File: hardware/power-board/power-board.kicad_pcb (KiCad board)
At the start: 2 copper layers, 144 parts, among them IC101 TCAN332DR, IC102 NUP2105LT1G, IC103 STM32C092KCT6, IC104 TPS62933DRLR, IC201 BQ7694202PFBR, IC301 BQ25798RQMR, IC302 CYPD3177-24LQXQ, J101 CAN, J102 SYSCTL, J103 TC2050, J201 XT60 BAT, J202 BALANCE, J203 NTC CELL, J204 POWER BTN, J205 XT30 LEFT, J206 XT30 RIGHT, J207 XT30 CARRIER, J301 USB4125-GF-A, Q101 2N7002, Q201 BSC010N04LSATMA1, Q202 DMP3099L, Q203 BSC010N04LSATMA1, Q204 BCP56, Q301 BSS138-7-F, Y101 Crystal_GND24

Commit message: updated power node pcb
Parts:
- moved R206 61.5 mm to (119.5, 72.5)
- moved IC201 60.3 mm to (105.0, 85.0)
- moved R203 56.0 mm to (119.5, 75.0)
- moved R211 55.6 mm to (113.0, 67.0), turned to 90 degrees
- moved R212 53.9 mm to (119.5, 80.0)
- moved R210 52.5 mm to (119.5, 77.5)
- moved R213 48.2 mm to (117.0, 68.0)
- moved R219 46.6 mm to (108.0, 71.0)
- moved R202 45.3 mm to (102.0, 67.0), turned to 90 degrees
- moved Q202 45.2 mm to (123.0, 77.0)
- moved R205 45.2 mm to (93.0, 68.0)
- moved TP302 42.4 mm to (87.0, 95.0)
- moved R214 42.3 mm to (123.0, 82.0)
- moved C206 42.1 mm to (125.0, 63.0)
- moved Q204 37.0 mm to (104.0, 70.5)
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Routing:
- added copper zone on F.Cu, net /BAT+
- added copper zone on F.Cu, net /PACK+
- added copper zone on B.Cu, net GND
- added copper zone on F.Cu, net GND
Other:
- board outline added: 65 x 65 mm

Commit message: changed power board to 4 layers
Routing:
- removed copper zone on F.Cu, net /BAT+
- removed copper zone on F.Cu, net /PACK+
- removed copper zone on B.Cu, net GND
- removed copper zone on F.Cu, net GND
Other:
- board outline removed
- copper layers 2 -> 4

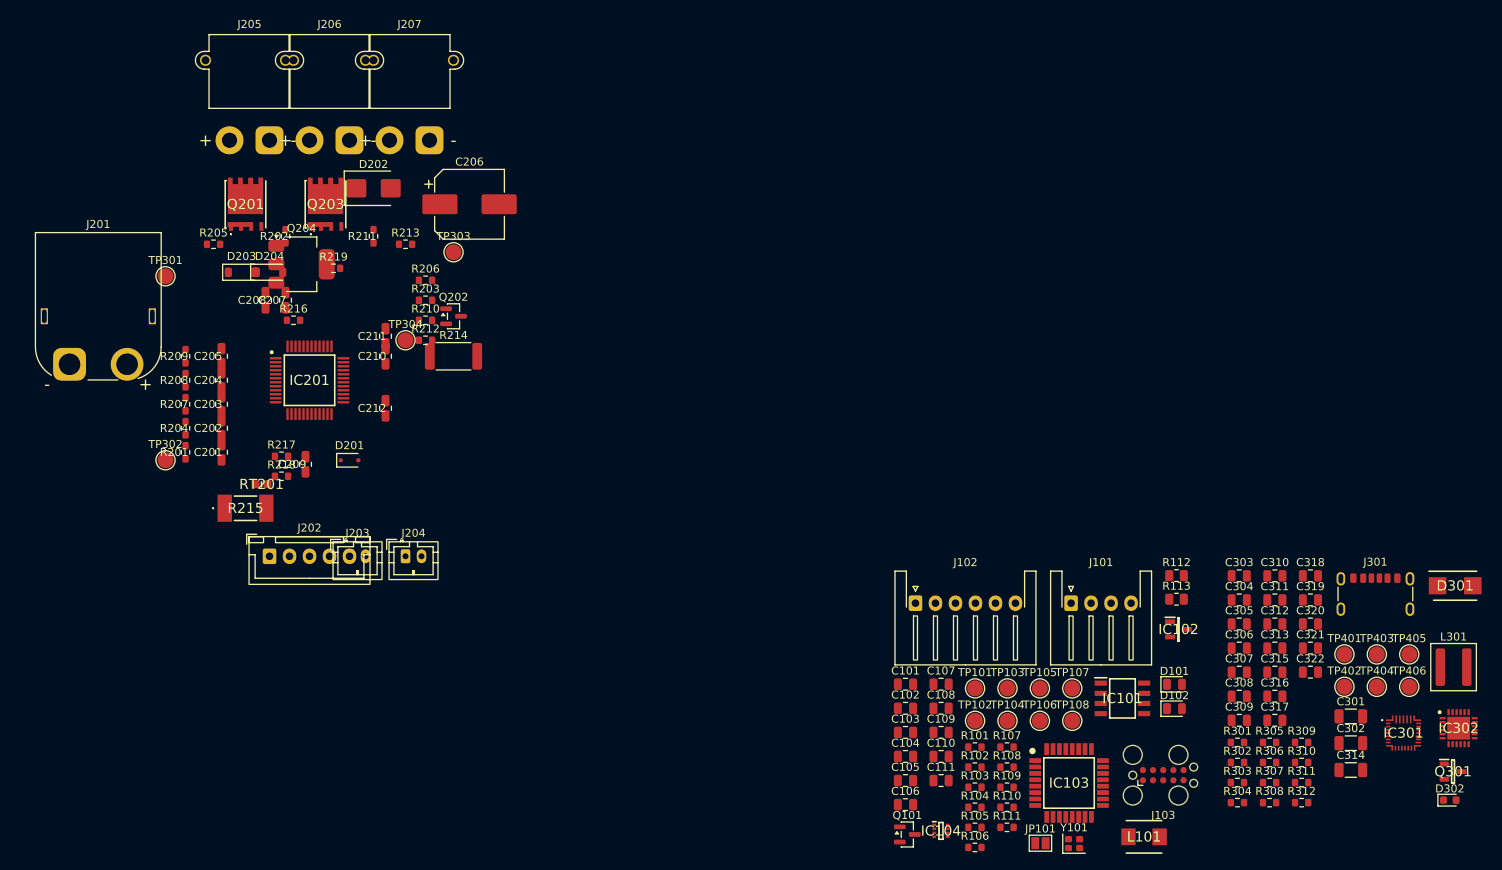
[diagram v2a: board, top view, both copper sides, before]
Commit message: placed bms and power path on power board
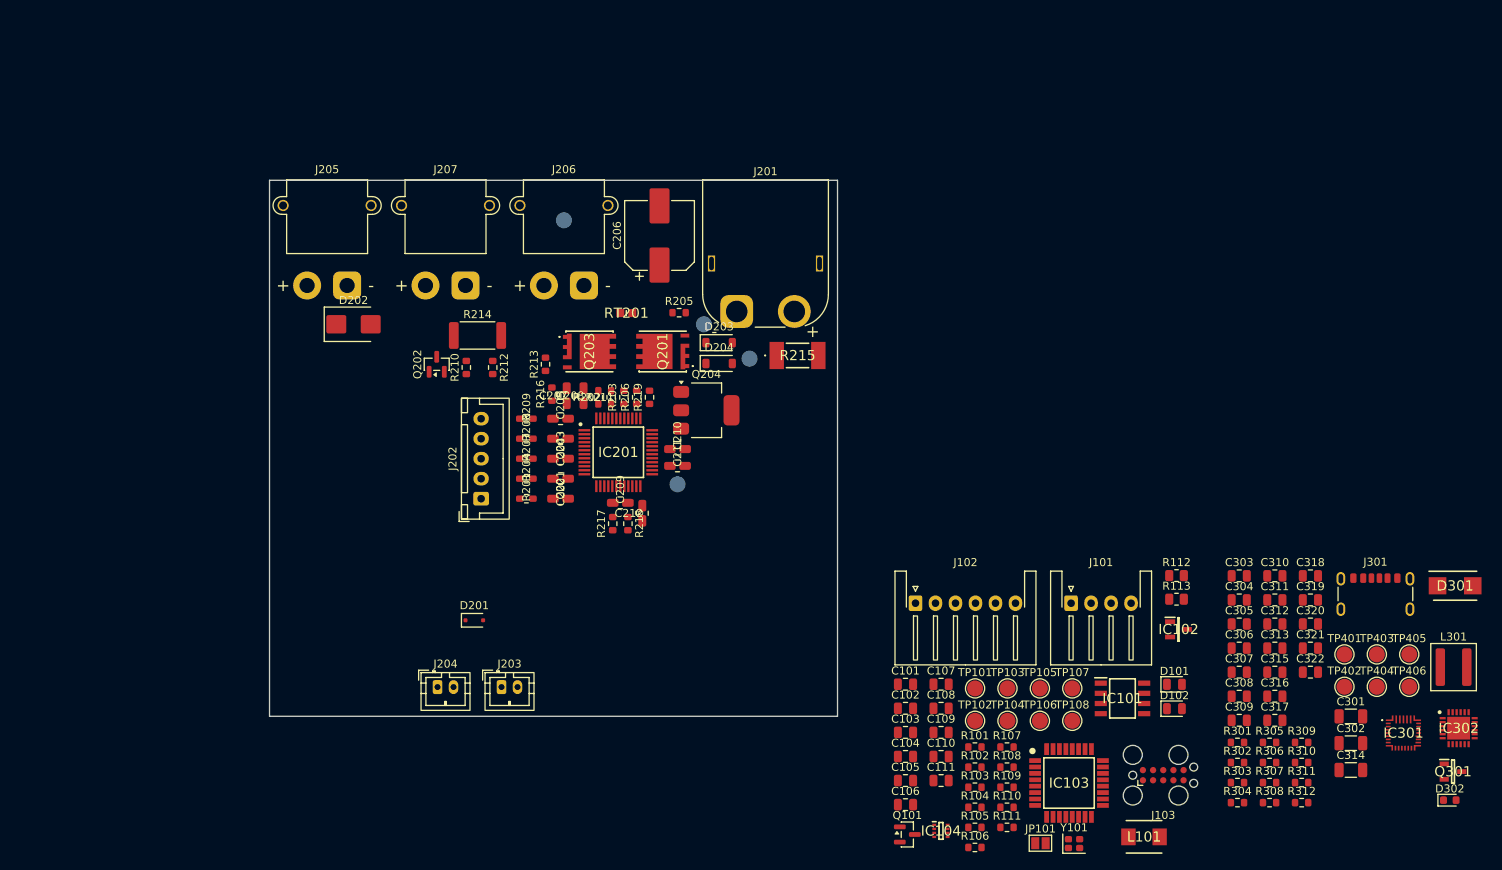
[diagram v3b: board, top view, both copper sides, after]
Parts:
- TP301, TP302, TP303, TP304: moved to B.Cu
- moved J201 83.7 mm to (158.4, 76.4)
- moved TP302 74.1 mm to (160.0, 82.3)
- moved R215 71.6 mm to (166.0, 81.9)
- moved TP301 67.6 mm to (154.3, 78.0)
- moved D203 60.3 mm to (156.2, 80.3)
- moved R205 58.8 mm to (151.2, 76.5)
- moved D204 57.3 mm to (156.2, 82.9)
- moved Q201 55.3 mm to (149.2, 81.4), turned to 90 degrees
- moved Q204 53.8 mm to (154.6, 88.8)
- moved RT201 50.4 mm to (144.6, 76.6)
- moved R202 44.0 mm to (141.1, 87.1)
- moved R218 43.7 mm to (144.8, 102.9), turned to -90 degrees
- moved R209 43.3 mm to (132.1, 89.8), turned to 0 degrees
- moved R208 43.2 mm to (132.1, 92.3), turned to 0 degrees
- moved R207 43.1 mm to (132.1, 94.8), turned to 0 degrees
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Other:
- board outline added: 71 x 67 mm

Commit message: placed charger on power board
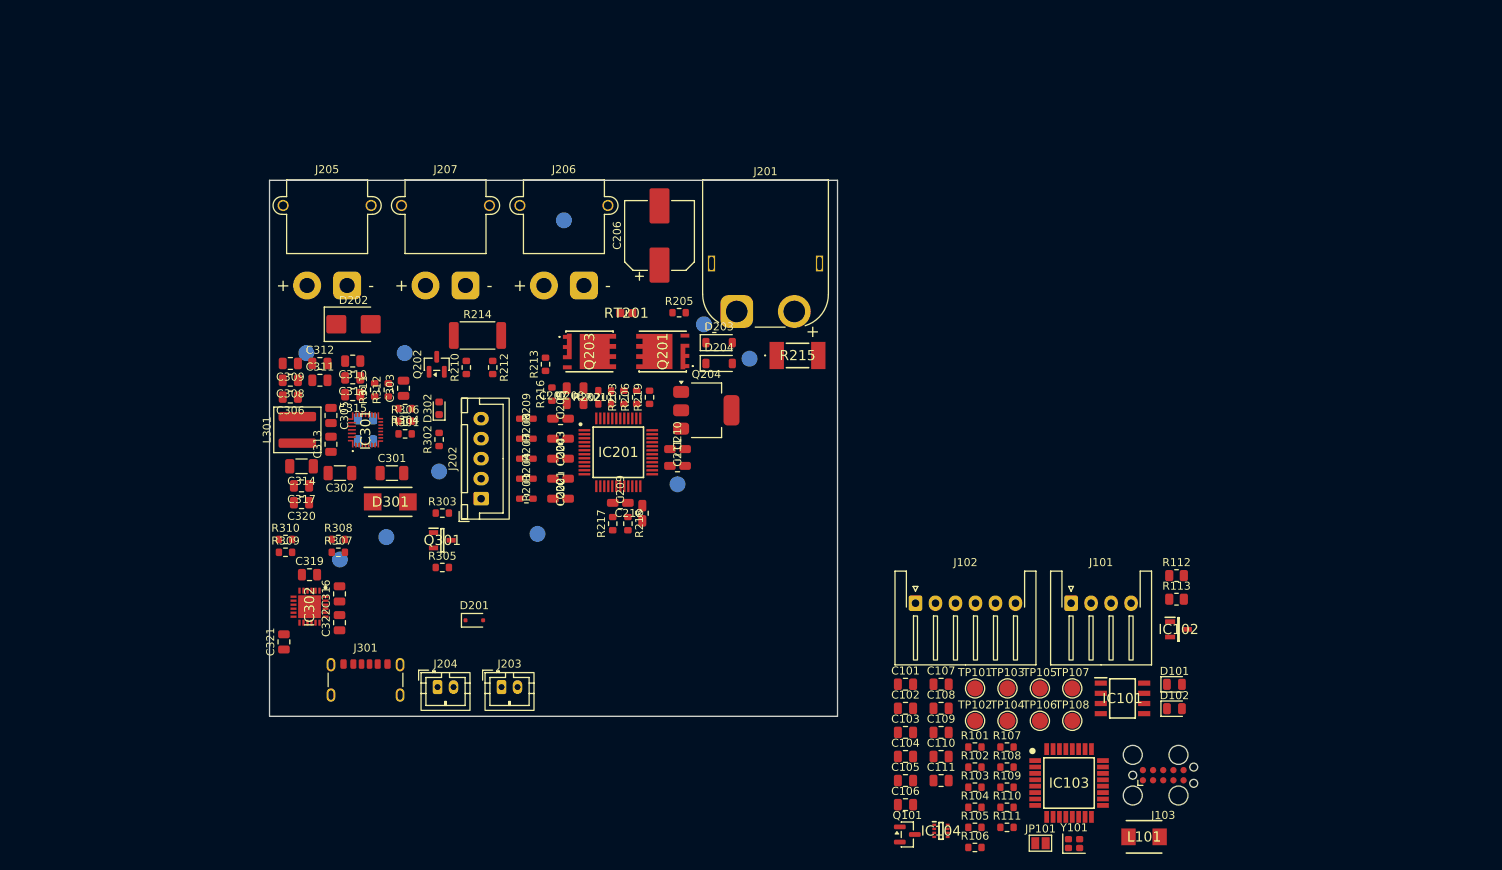
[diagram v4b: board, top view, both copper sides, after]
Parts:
- C304, C307, TP401, TP402, TP403, TP404, TP405, TP406: moved to B.Cu
- moved L301 147.5 mm to (103.5, 91.2), turned to 90 degrees
- moved IC302 144.4 mm to (105.0, 113.3), turned to -90 degrees
- moved TP403 139.0 mm to (104.6, 81.6)
- moved C314 136.5 mm to (104.0, 95.8), turned to 180 degrees
- moved D302 135.5 mm to (121.2, 88.5), turned to 90 degrees
- moved IC301 135.2 mm to (112.0, 91.2), turned to 90 degrees
- moved D301 133.5 mm to (115.1, 100.2)
- moved C302 130.8 mm to (108.8, 96.6), turned to 180 degrees
- moved TP404 130.6 mm to (108.8, 107.4)
- moved R310 130.0 mm to (102.0, 104.9)
- moved Q301 129.6 mm to (121.6, 105.0)
- moved R309 129.2 mm to (102.0, 106.5)
- moved C321 128.3 mm to (101.8, 117.7), turned to 90 degrees
- moved C320 127.0 mm to (104.0, 100.3), turned to 180 degrees
- moved C309 126.7 mm to (102.6, 82.9), turned to 180 degrees
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
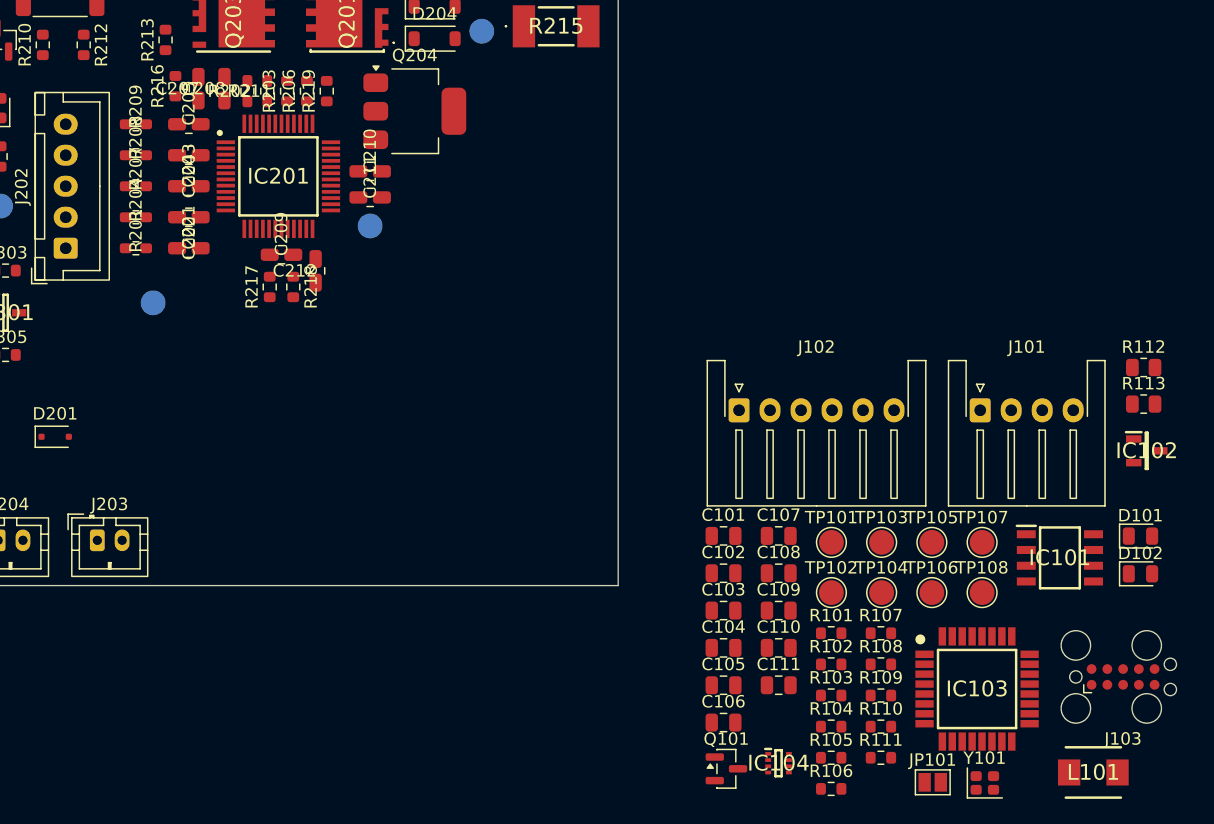
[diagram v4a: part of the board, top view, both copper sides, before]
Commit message: placed mcu, can and 3v3 buck on power board
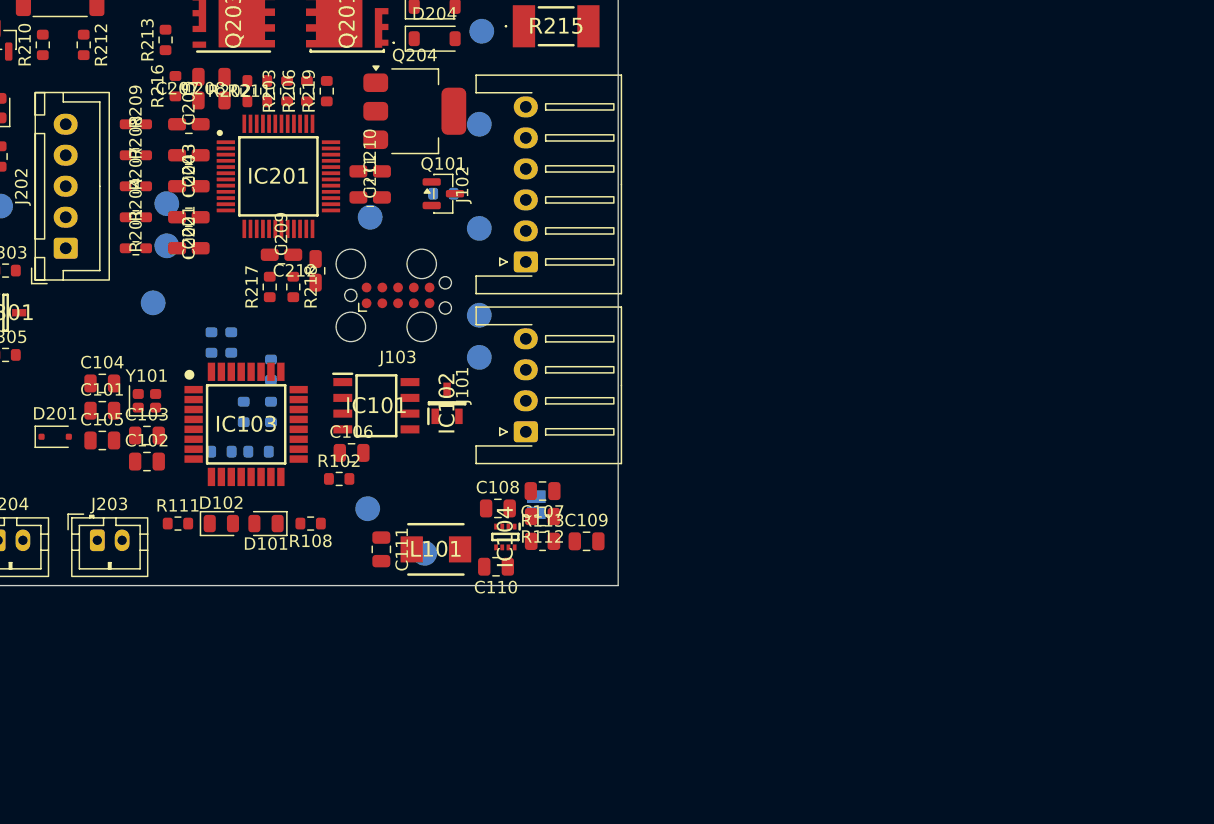
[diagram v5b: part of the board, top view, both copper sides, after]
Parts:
- JP101, R101, R103, R104, R105, R106, R107, R109, R110, TP101, TP102, TP103, TP104, TP105, TP106, TP107, TP108: moved to B.Cu
- moved Y101 74.3 mm to (133.0, 112.1)
- moved D102 74.2 mm to (139.0, 122.0)
- moved TP107 71.2 mm to (134.6, 96.2)
- moved D101 70.5 mm to (142.6, 122.0), turned to 180 degrees
- moved TP106 67.7 mm to (134.6, 99.6)
- moved J103 66.1 mm to (153.2, 103.6)
- moved IC103 62.7 mm to (141.0, 114.0)
- moved R110 62.2 mm to (138.2, 107.4), turned to 90 degrees
- moved R111 59.7 mm to (135.5, 122.0)
- moved R109 59.6 mm to (139.8, 107.4), turned to 90 degrees
- moved IC102 56.6 mm to (157.2, 112.3), turned to 90 degrees
- moved IC101 56.5 mm to (151.5, 112.5)
- moved R106 56.3 mm to (140.8, 113.0), turned to 90 degrees
- moved L101 56.0 mm to (156.3, 124.1), turned to 180 degrees
- moved TP108 55.4 mm to (159.8, 89.8)
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
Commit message: moved bat diodes and sdrv cap on power board
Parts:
- C310: moved to B.Cu
- moved C310 4.84 mm to (108.0, 86.8), turned to 90 degrees
- moved D204 1.82 mm to (157.3, 81.5), turned to 90 degrees
- moved D203 1.81 mm to (154.8, 81.5), turned to 90 degrees

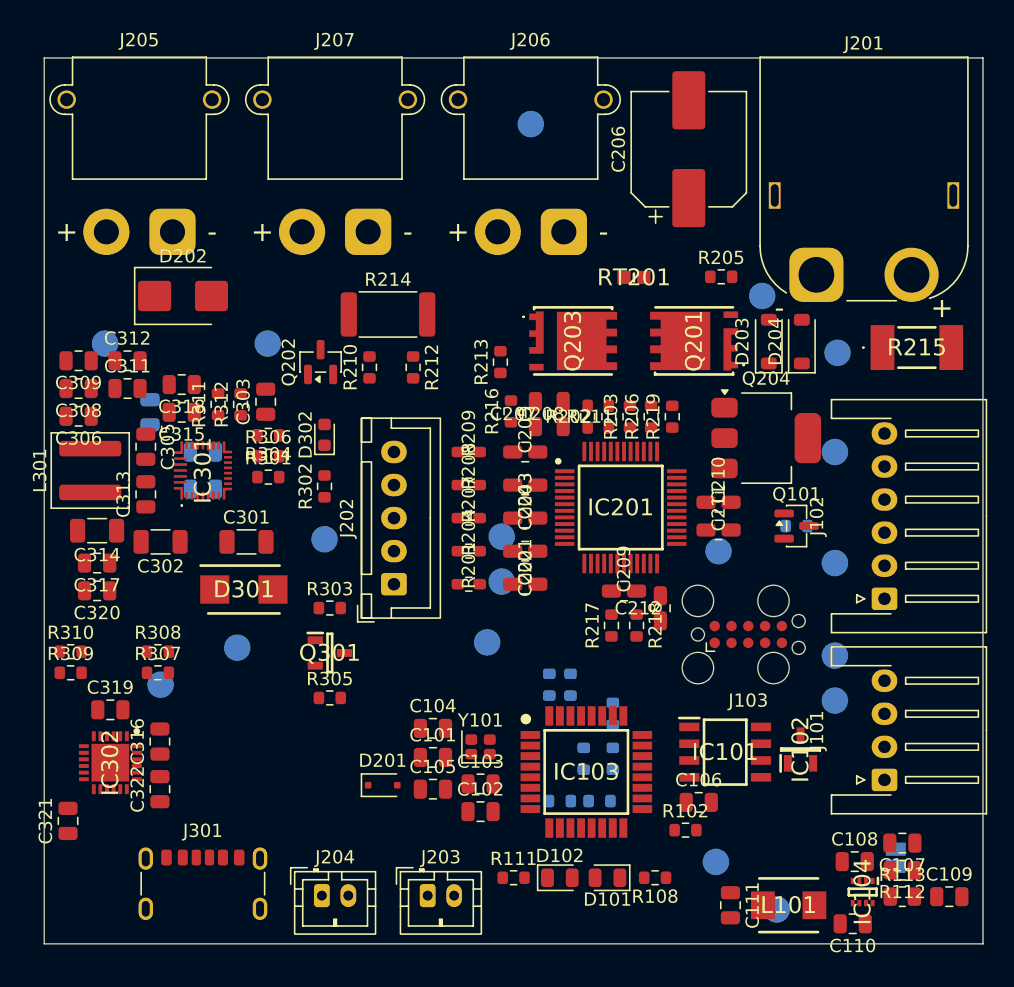
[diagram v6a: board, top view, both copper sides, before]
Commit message: added zone fills on power board
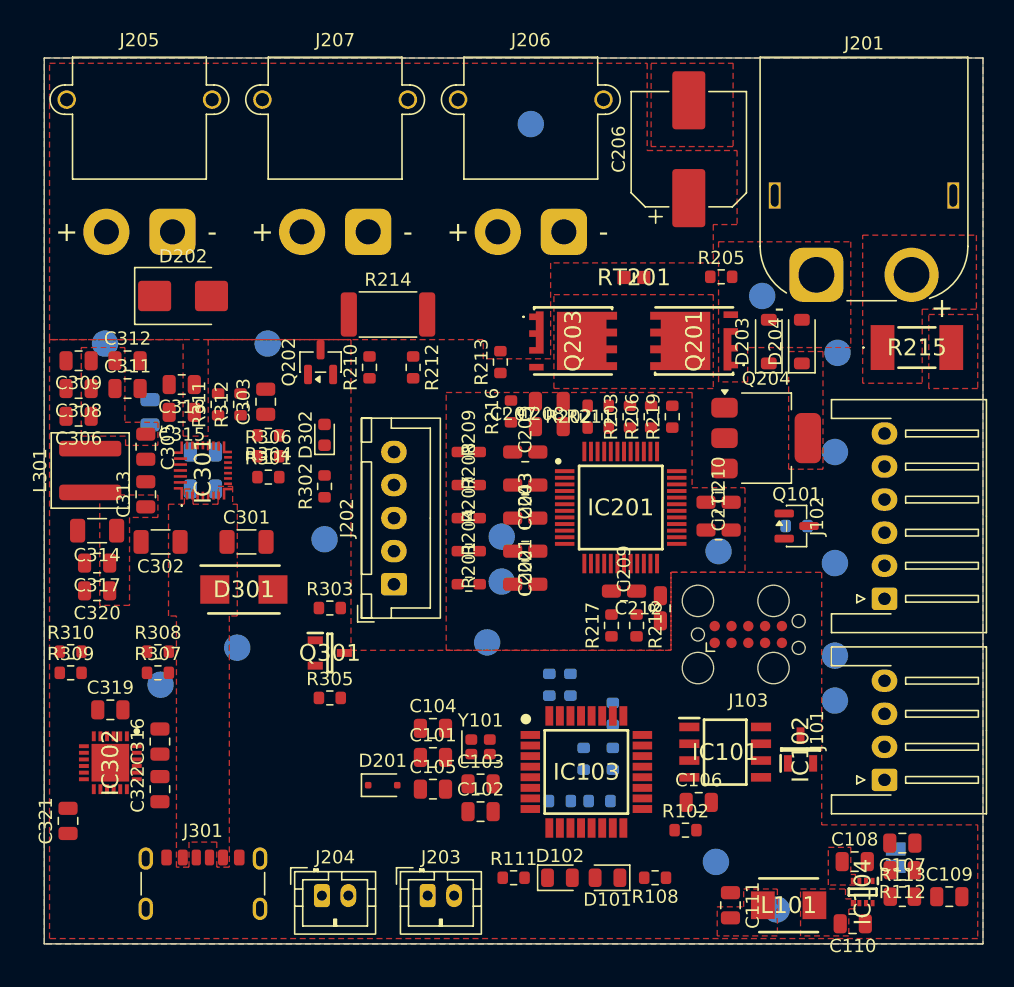
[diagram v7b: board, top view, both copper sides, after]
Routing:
- added copper zone on F.Cu, net +3V3
- added copper zone on In2.Cu, net +3V3
- added copper zone on F.Cu, net /BAT+
- added copper zone on In2.Cu, net /BAT+
- added copper zone on F.Cu, net /BMS/BAT-
- added copper zone on In1.Cu, net /BMS/BAT-
- added copper zone on In2.Cu, net /BMS/BAT-
- added copper zone on F.Cu, net /BMS/BMS_REG0_C
- added copper zone on F.Cu, net /BMS/FET_MID
- added copper zone on In2.Cu, net /BMS/FET_MID
- added copper zone on F.Cu, net /Charger/CHG_PMID
- added copper zone on F.Cu, net /Charger/CHG_SYS
- added copper zone on F.Cu, net /Charger/VBUS
- added copper zone on F.Cu, net /PACK+
- added copper zone on In2.Cu, net /PACK+
- added copper zone on B.Cu, net GND
- added copper zone on F.Cu, net GND
- added copper zone on In1.Cu, net GND
- added copper zone on In2.Cu, net GND
- added copper zone on F.Cu, net Net-(IC104-SW)

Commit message: rerouted on the powerboard
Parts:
- moved C302 2.30 mm to (108.8, 98.9)
- moved C313 2.00 mm to (107.7, 95.0), turned to -90 degrees
- moved C305 1.60 mm to (107.6, 87.8)
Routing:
- net GND: track 0.00 -> 51.8 mm, vias 0 -> 24
- net /BMS/BAT-: track 0.00 -> 47.0 mm, vias 0 -> 2
- net /Charger/CHG_SW1: track 0.00 -> 6.79 mm, vias 0 -> 1
- net /Charger/CHG_SW2: track 0.00 -> 6.67 mm, vias 0 -> 1
- net /Charger/CHG_SYS: track 0.00 -> 4.62 mm
- net /Charger/VBUS: track 0.00 -> 4.05 mm
- net /BMS/BMS_SRP: track 0.00 -> 3.11 mm
- net /BMS/BMS_SRN: track 0.00 -> 3.11 mm
- net /Charger/CHG_PMID: track 0.00 -> 2.80 mm
- net /PACK+: track 0.00 -> 1.00 mm
